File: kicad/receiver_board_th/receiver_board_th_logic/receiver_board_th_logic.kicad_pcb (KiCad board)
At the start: 2 copper layers, 31 x 36 mm, 11 parts, among them J1 B2B 1, J2 B2B 2, J4 Debug, J5 Battery Conn, Q1 FQP27P06, SW1 On/Off, SW2 Pair/Direction, U1 5V Buck

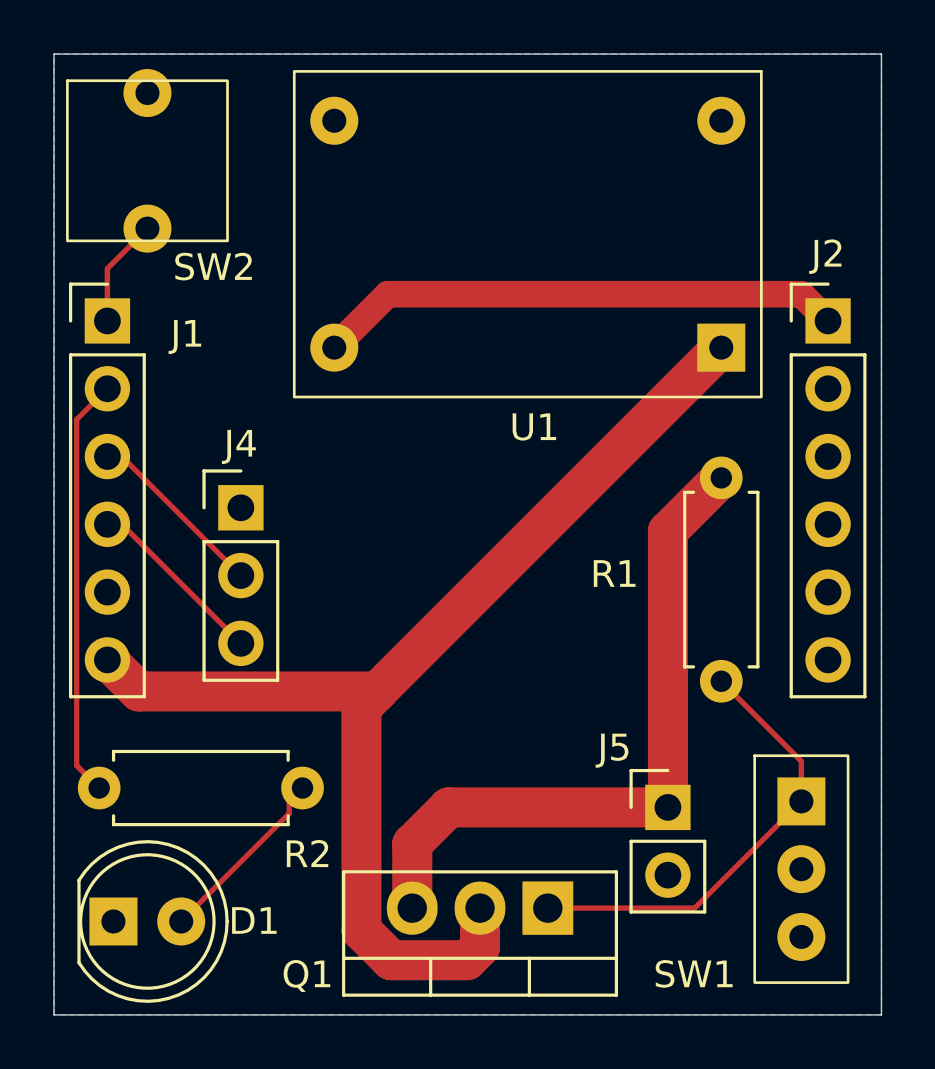
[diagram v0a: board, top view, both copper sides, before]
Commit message: Investigating a SMD version of receiver board, so renaming existing projects with _th and reorganizing
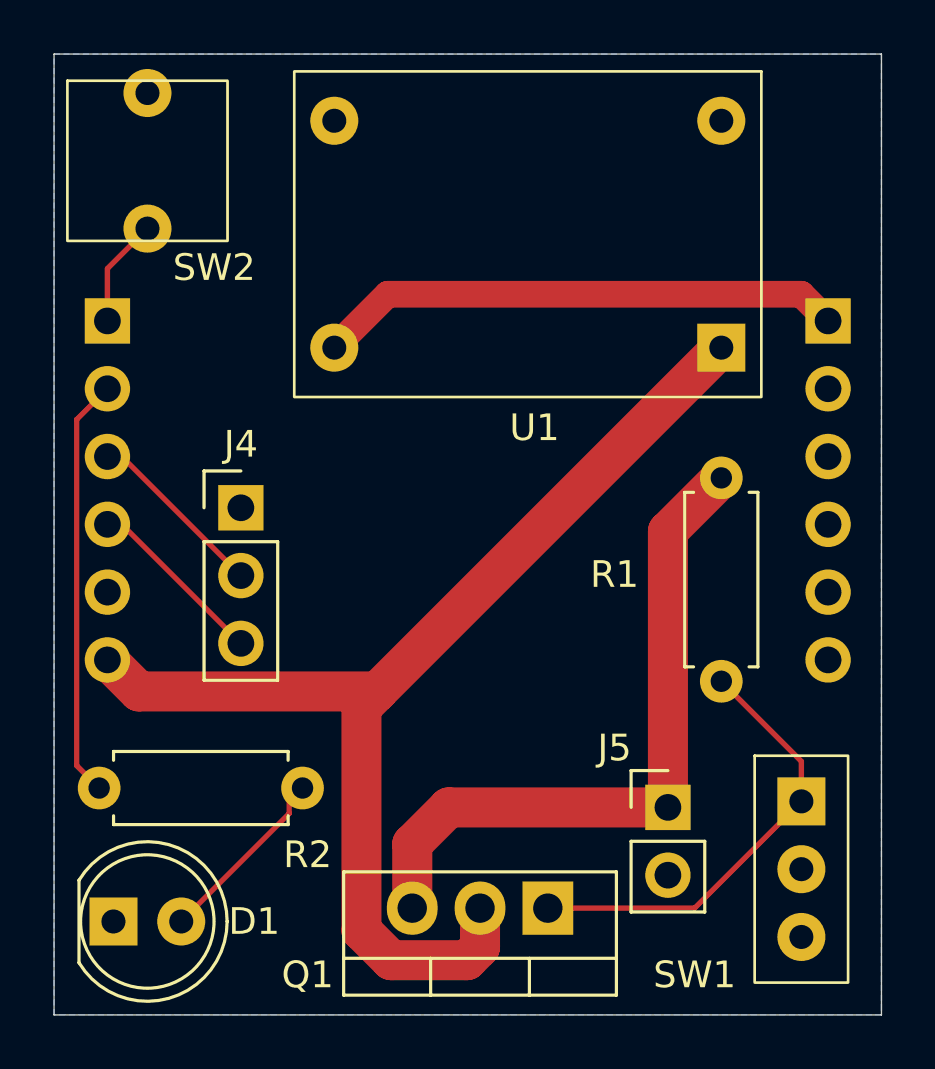
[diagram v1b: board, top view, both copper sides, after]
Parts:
- J1, J2: moved to B.Cu
- turned J1 to 180 degrees
- turned J2 to 180 degrees

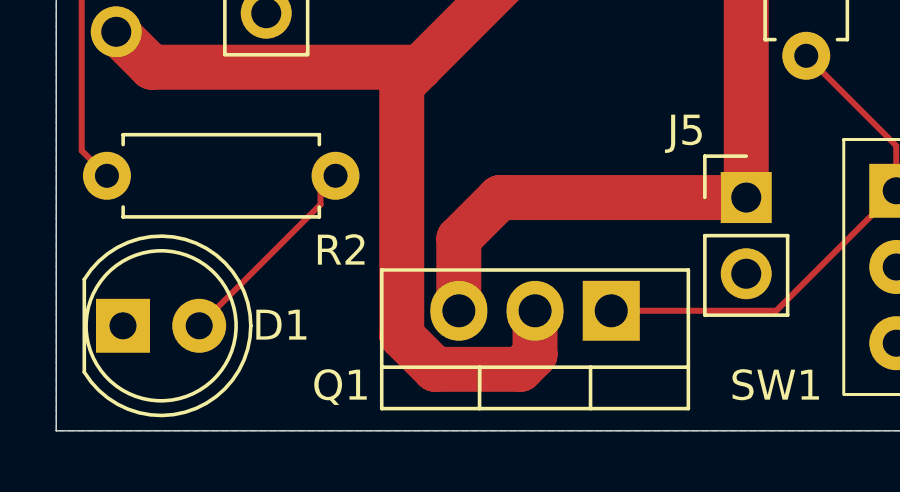
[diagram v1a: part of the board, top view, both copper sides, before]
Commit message: Add M2 mounting holes to receiver power board
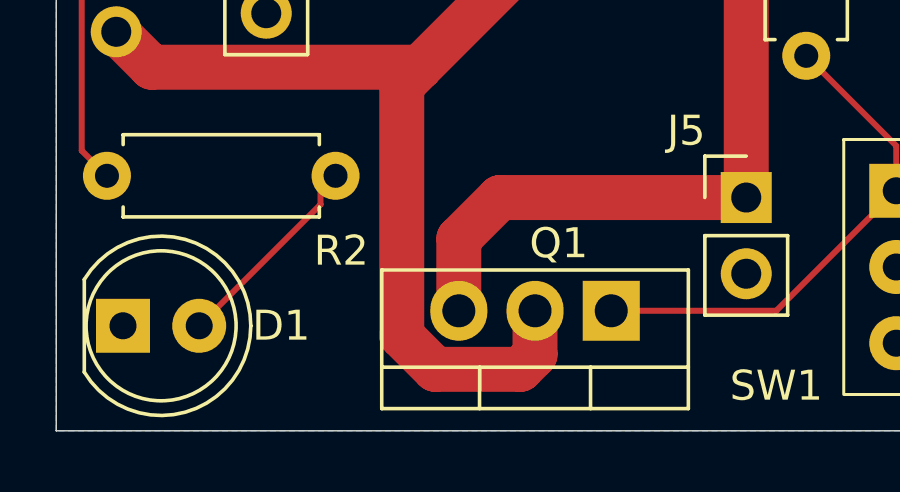
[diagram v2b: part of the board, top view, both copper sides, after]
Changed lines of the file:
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@@
 		(tags "TO-220-3 Vertical RM 2.54mm")
 		(property "Reference" "Q1"
-			(at 9 -2.5 0)
+			(at 1.75 2.25 0)
 			(layer "F.SilkS")
 			(effects
@@
 		(tags "Through hole pin header THT 1x06 2.54mm single row")
 		(property "Reference" "J2"
-			(at 0 2.5 0)
+			(at -0.5 2.5 0)
 			(layer "B.SilkS")
 			(effects
@@
 		(tags "Through hole pin header THT 1x06 2.54mm single row")
 		(property "Reference" "J1"
-			(at 3 -0.5 0)
+			(at 0.5 2.5 0)
 			(layer "B.SilkS")
 			(effects
